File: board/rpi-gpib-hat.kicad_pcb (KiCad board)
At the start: 2 copper layers, 65 x 30 mm, 73 parts, among them J1 RPI_GPIO, J2 GPIB, U1 SN75162BDW, U2 SN75160BDW, U3 CAT24C32

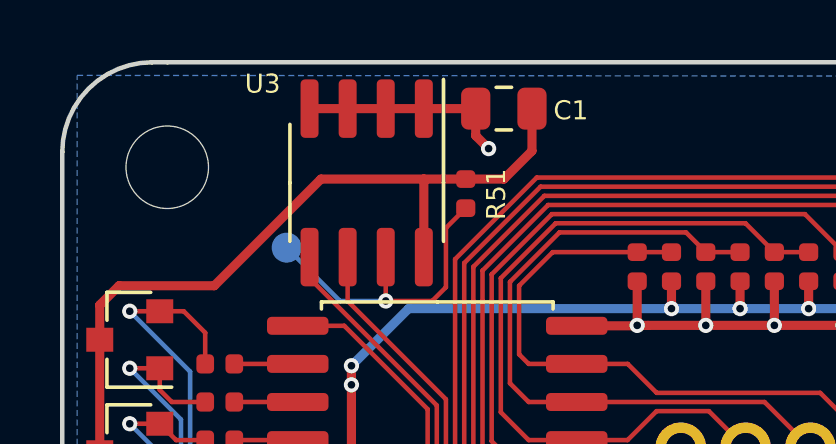
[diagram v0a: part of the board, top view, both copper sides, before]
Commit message: License hardware under CERN OHL v1.2.
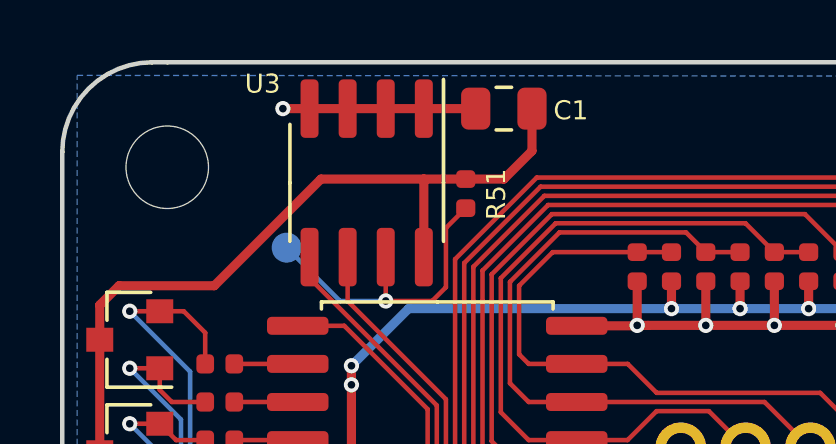
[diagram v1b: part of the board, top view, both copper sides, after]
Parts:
- moved OSHW 0.89 mm to (106.9, 100.0)
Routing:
- net GND: track 149.2 -> 148.5 mm
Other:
- board text added: "Raspberry Pi GPIB µHAT v0.1"
- board text added: "https://github.com/Elemecca/rpi-gpib Licensed under CERN OHL v1.2"
- board text removed: "Raspberry Pi GPIB µHAT v0.1 github.com/Elemecca/rpi-gpib"
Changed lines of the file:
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@@
   (general
     (thickness 1.6)
-    (drawings 28)
-    (tracks 729)
+    (drawings 29)
+    (tracks 728)
     (zones 0)
     (modules 73)
@@
   (page A4)
   (title_block
-    (title "Raspberry Pi Zero (W) uHAT Template Board")
-    (date 2019-02-28)
-    (rev 1.0)
-    (comment 1 "This PCB design is licensed under MIT Open Source License.")
+    (title "Raspberry Pi GPIB µHAT")
+    (date 2019-05-17)
+    (rev 0.1)
+    (company "© 2019 Sam Hanes. Licensed under CERN OHL v1.2.")
+    (comment 1 https://github.com/Elemecca/rpi-gpib)
   )
   (layers
@@
       (solder_mask_margin 1.75) (clearance 2))
   )
-  (module local:OSHW locked (layer B.Cu)
-    (at 106 100)
+  (module local:OSHW (layer B.Cu)
+    (at 106.889 100)
     (descr "Imported from /home/sam/Downloads/oshw.svg")
     (tags svg2mod)
@@
     )
   )
+  (gr_text "Raspberry Pi GPIB µHAT v0.1" (at 109.315 101.156 180) (layer B.SilkS)
+    (effects (font (size 0.889 0.889) (thickness 0.1524)) (justify left mirror))
+  )
   (gr_text "D5...D8\nR41...R48" (at 156.051 118.301 270) (layer F.SilkS)
     (effects (font (size 0.635 0.635) (thickness 0.1524)))
@@
   (gr_line (start 154.95 119.91) (end 161.05 119.91) (layer F.CrtYd) (width 0.05))
   (gr_line (start 154.95 113.81) (end 161.05 113.81) (layer F.CrtYd) (width 0.05))
-  (gr_text "Raspberry Pi GPIB µHAT v0.1\ngithub.com/Elemecca/rpi-gpib" (at 108.5 100 180) (layer B.SilkS)
-    (effects (font (size 1 1) (thickness 0.15)) (justify left mirror))
+  (gr_text "https://github.com/Elemecca/rpi-gpib\nLicensed under CERN OHL v1.2" (at 109.389 99.251 180) (layer B.SilkS)
+    (effects (font (size 0.635 0.635) (thickness 0.1524)) (justify left mirror))
   )
   (gr_text "Board Corner Radius = 3mm\nAll holes are M2.5" (at 184.278 127.334) (layer Cmts.User)
@@
   (segment (start 107.41 115.507) (end 107.41 114.8466) (width 0.3048) (layer F.Cu) (net 3))
   (segment (start 115.665 105.270801) (end 115.665 103.8) (width 0.3048) (layer F.Cu) (net 3) (status 20))
-  (via (at 110.712 99.378) (size 0.508) (drill 0.254) (layers F.Cu B.Cu) (net 3))
-  (segment (start 110.2825 98.046) (end 110.2825 98.9485) (width 0.3048) (layer F.Cu) (net 3) (status 10))
-  (segment (start 110.2825 98.9485) (end 110.712 99.378) (width 0.3048) (layer F.Cu) (net 3))
   (via (at 142.335 116.777) (size 0.508) (drill 0.254) (layers F.Cu B.Cu) (net 3))
   (segment (start 142.335 117.666) (end 142.335 116.777) (width 0.3048) (layer F.Cu) (net 3))
   (segment (start 144.35 117.985) (end 142.654 117.985) (width 0.3048) (layer F.Cu) (net 3) (status 10))
   (segment (start 142.654 117.985) (end 142.335 117.666) (width 0.3048) (layer F.Cu) (net 3))
+  (via (at 103.854 98.046) (size 0.508) (drill 0.254) (layers F.Cu B.Cu) (net 3))
+  (segment (start 103.854 98.046) (end 104.743 98.046) (width 0.3048) (layer F.Cu) (net 3))
   (via (at 137.89 117.05632) (size 0.508) (drill 0.254) (layers F.Cu B.Cu) (net 4) (status 40000))
   (segment (start 137.89 121.73) (end 137.89 117.05632) (width 0.1524) (layer F.Cu) (net 4) (status 10))

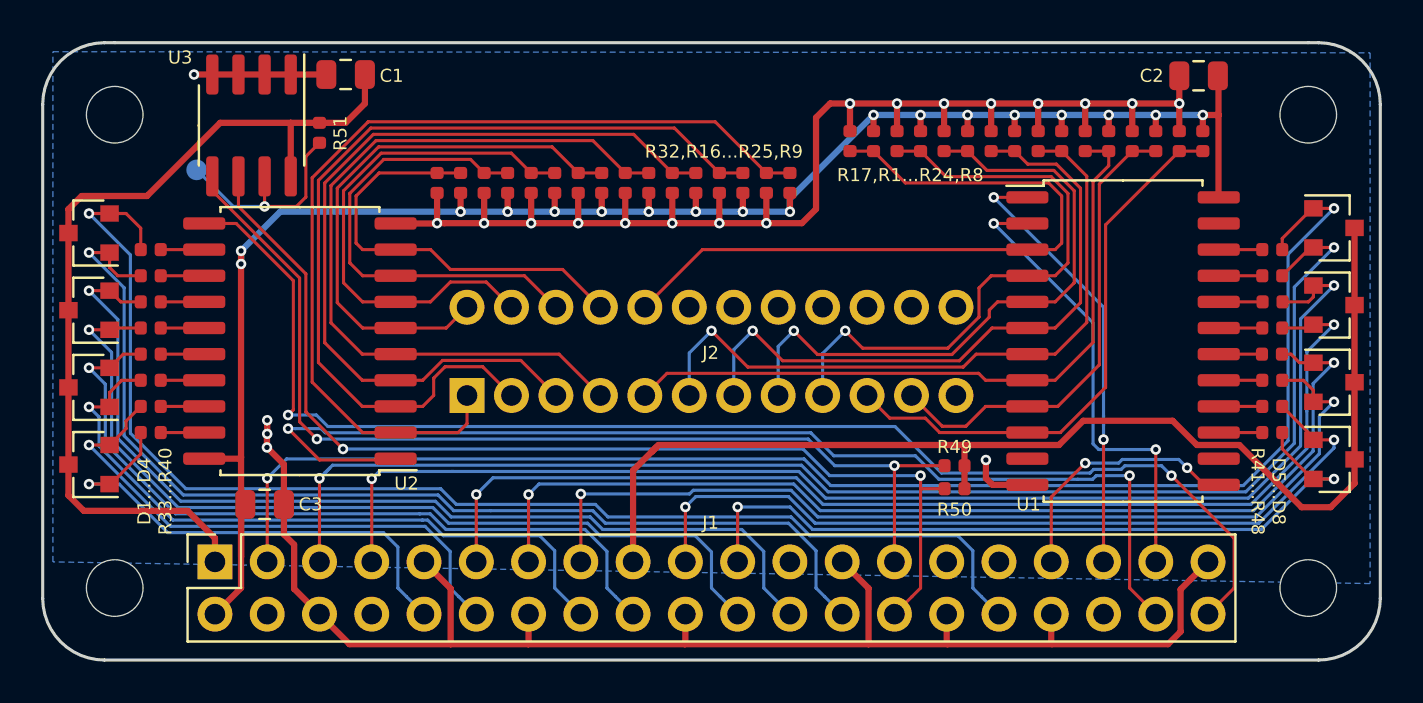
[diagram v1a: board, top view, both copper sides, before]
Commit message: Add 2.5V regulator for diode clamps.
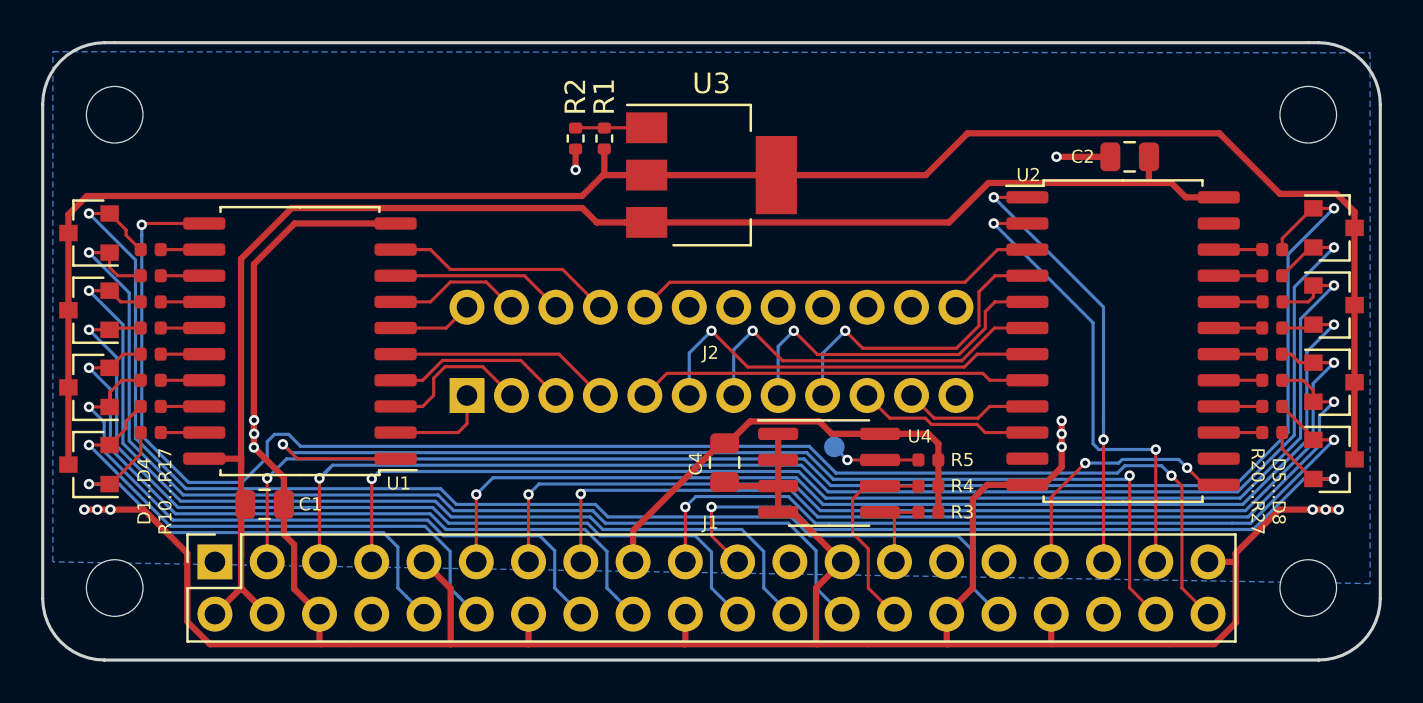
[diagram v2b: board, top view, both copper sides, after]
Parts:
- removed the R10 at (130.5, 103.3)
- removed the R11 at (128.2, 103.3)
- removed the R12 at (126.0, 103.3)
- removed the R13 at (123.7, 103.3)
- removed the R14 at (121.4, 103.3)
- removed the R15 at (119.1, 103.3)
- removed the R16 at (116.8, 103.3)
- removed the R17 at (135.7, 101.3)
- removed R18, R19, R28, R29, R30, R31, R32: 6k2, Resistor_SMD:R_0402_1005Metric
- removed the R20 at (142.6, 101.3)
- removed the R21 at (144.9, 101.3)
- removed the R22 at (147.2, 101.3)
- removed the R23 at (149.4, 101.3)
- removed the R24 at (151.7, 101.3)
- removed the R25 at (131.7, 103.3)
- removed the R26 at (129.4, 103.3)
- removed the R27 at (127.1, 103.3)
- removed the R3 at (141.4, 101.3)
- removed the R4 at (143.7, 101.3)
- removed the R5 at (146.0, 101.3)
- removed R6, R7, R8, R9: 3k, Resistor_SMD:R_0402_1005Metric
- added U3: LM317_SOT-223, Package_TO_SOT_SMD:SOT-223-3_TabPin2, F.Cu at (129.0, 102.9)
- R1, R2: value 3k -> 100
- TP1: value WP -> TestPoint
- moved TP1 33.8 mm to (135.0, 116.1)
- moved R5 33.6 mm to (139.5, 116.8), turned to 180 degrees
- moved U4 32.8 mm to (134.7, 117.4), turned to 0 degrees
- moved C4 26.4 mm to (129.6, 116.9), turned to 270 degrees
- moved R2 16.8 mm to (122.4, 101.2), turned to 270 degrees
- moved R1 13.1 mm to (123.8, 101.2)
- moved C2 5.17 mm to (149.3, 102.0)
- moved R3 2.59 mm to (139.5, 119.3)
- moved R4 1.28 mm to (139.5, 118.0)
- renumbered C3 to C1, C1 to C4, R33 to R10, R34 to R11, R35 to R12, R36 to R13, R37 to R14, R38 to R15, R39 to R16, R40 to R17, R41 to R20, R42 to R21, R43 to R22, R44 to R23, R45 to R24, R46 to R25, R47 to R26, R48 to R27, R49 to R3, R50 to R4, R51 to R5, U2 to U1, U1 to U2, U3 to U4
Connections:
- D1 pad 3: +3V3 -> +2V5
- D2 pad 3: +3V3 -> +2V5
- D3 pad 3: +3V3 -> +2V5
- D4 pad 3: +3V3 -> +2V5
- D5 pad 3: +3V3 -> +2V5
- D6 pad 3: +3V3 -> +2V5
- D7 pad 3: +3V3 -> +2V5
- D8 pad 3: +3V3 -> +2V5
- J1 pad 23: (no net) -> /GPIO11
- J1 pad 29: (no net) -> /GPIO5
- J1 pad 31: (no net) -> /GPIO6
- J1 pad 36: (no net) -> /GPIO16
- J1 pad 8: (no net) -> /GPIO14
- J2 pad 12: (no net) -> Earth_Clean
- R1 pad 1: /REN -> +2V5
- R1 pad 2: +5V -> Net-(R1-Pad2)
- R2 pad 1: /IFC -> Net-(R1-Pad2)
- R2 pad 2: +5V -> GND
- U2 pad 11: (no net) -> Net-(U2-Pad11)
- U2 pad 14: (no net) -> Net-(U2-Pad14)
- U2 pad 23: (no net) -> Net-(U2-Pad23)
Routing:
- net +2V5: track 0.00 -> 92.2 mm
- net +3V3: track 101.2 -> 22.3 mm
- net /ID_SD: track 50.6 -> 4.15 mm, vias 2 -> 0
- net /ID_SC: track 52.6 -> 10.0 mm, vias 2 -> 0
- net /DIO1: track 45.7 -> 5.02 mm
- net /DIO2: track 43.6 -> 7.50 mm
- net /DIO3: track 40.6 -> 8.90 mm
- net /DIO4: track 38.2 -> 10.8 mm
- net /DIO5: track 27.0 -> 3.89 mm
- net /SRQ: track 27.4 -> 8.54 mm
- net /DIO6: track 25.3 -> 6.54 mm
- net /ATN: track 23.2 -> 6.32 mm
- net +5V: track 93.4 -> 77.1 mm, vias 18 -> 0
- net /REN: track 35.0 -> 19.7 mm
- net /EOI: track 33.9 -> 19.2 mm
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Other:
- board text added: "D1...D4 R10...R17"
- board text added: "D5...D8 R20...R27"
- board text added: "Raspberry Pi GPIB µHAT v0.2"
- board text added: "https://github.com/elemecca/rpi-gpib Licensed under CERN OHL v1.2"
- board text removed: "D1...D4 R33...R40"
- board text removed: "D5...D8 R41...R48"
- board text removed: "R17,R1...R24,R8"
- board text removed: "R32,R16...R25,R9"
- board text removed: "Raspberry Pi GPIB µHAT v0.1"
- board text removed: "https://github.com/Elemecca/rpi-gpib Licensed under CERN OHL v1.2"

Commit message: Clean up routing.
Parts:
- moved TP1 0.18 mm to (134.8, 116.0)
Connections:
- U1 pad 1: /GPIO20 -> /GPIO21
- U1 pad 11: /GPIO21 -> /GPIO20
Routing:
- net /GPIO21: track 74.3 -> 43.8 mm, vias 2 -> 1
- net /GPIO20: track 55.0 -> 67.3 mm, vias 2 -> 1
- net /GPIO24: track 36.9 -> 43.5 mm
- net +5V: track 77.1 -> 74.1 mm
- net /GPIO19: track 22.1 -> 20.1 mm, vias 2 -> 0
- net /GPIO9: track 38.8 -> 40.3 mm
- net /GPIO22: track 46.9 -> 45.8 mm
- net /GPIO10: track 39.9 -> 41.0 mm
- net /GPIO2: track 71.1 -> 71.9 mm
- net /GPIO4: track 62.4 -> 63.1 mm
- net /GPIO13: track 12.6 -> 13.2 mm, vias 2 -> 0
- net +3V3: track 22.3 -> 22.9 mm
- net /GPIO26: track 23.1 -> 23.3 mm, vias 2 -> 0
